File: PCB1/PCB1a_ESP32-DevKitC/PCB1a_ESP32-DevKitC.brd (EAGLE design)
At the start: 125.6 x 84.2 mm, 26 parts, among them J1 691357310006B, J2 618009231421, J3 ESP32_DEVC_MIN_LEFT, J4 ESP32_DEVC_MIN_RIGHT, U2 MAX232D, U4 TLE9250VSJ, U8 74AHCT245, U9 74AHCT245

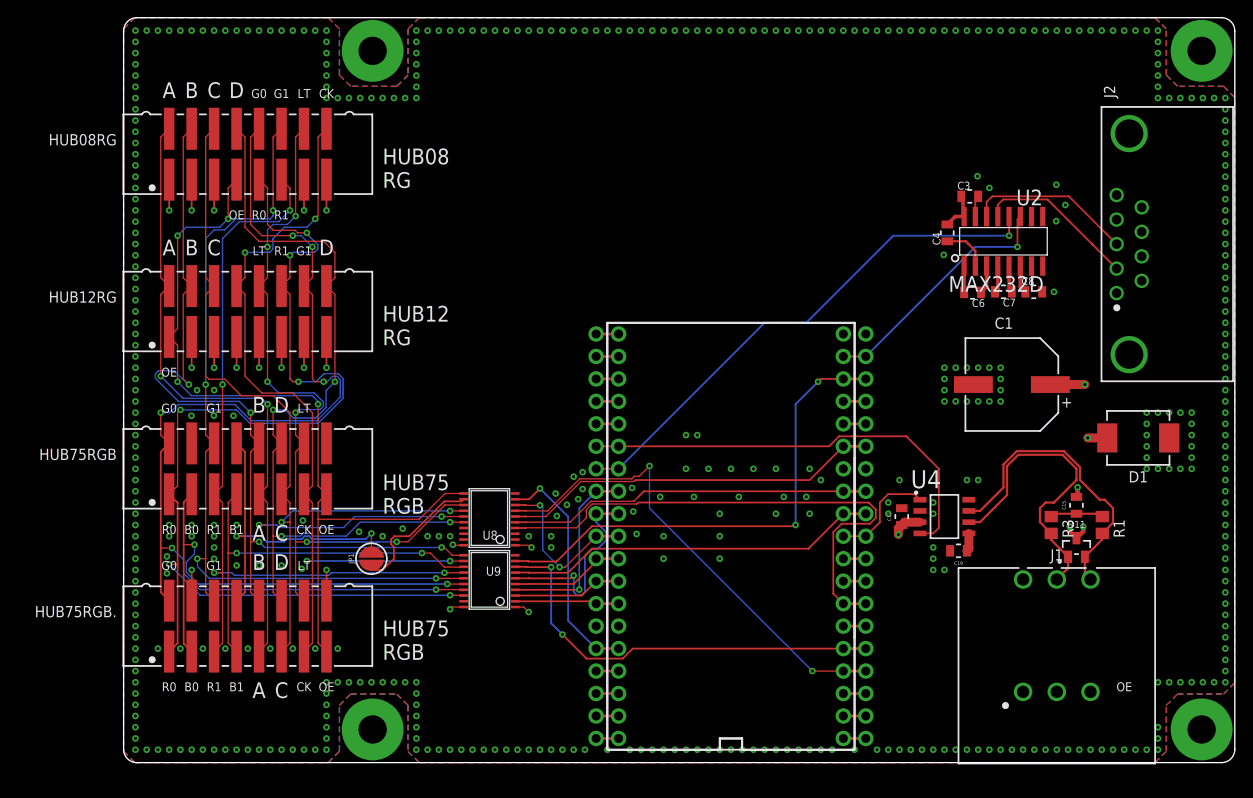
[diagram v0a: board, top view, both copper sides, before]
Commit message: SMD Connectors.
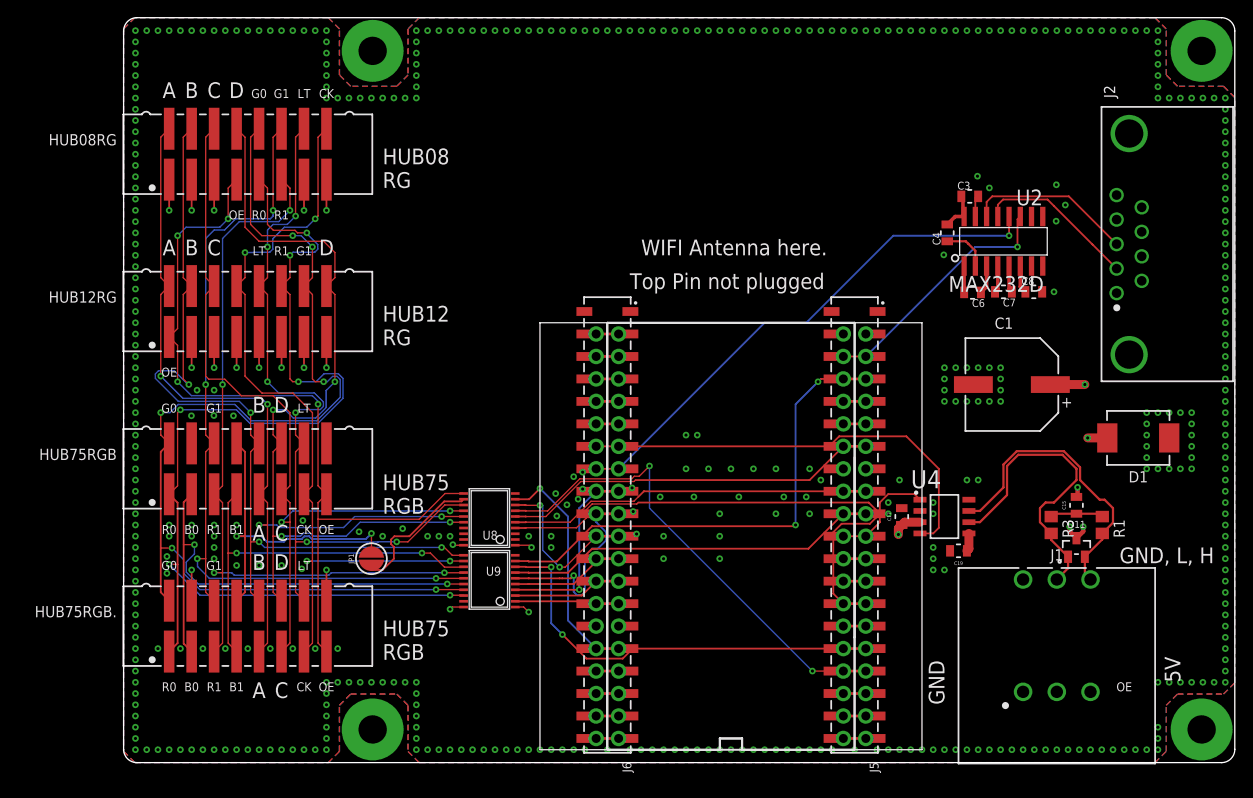
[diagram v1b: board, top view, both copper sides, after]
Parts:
- added J5, J6: 61004021821, Wurth_Connectors_WR-PHD:61004021821
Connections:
- new net N$12: J5.1, J5.2
- new net N$18: J6.1, J6.2
- new net N$4: J3.GND1A, J3.GND1B, J5.3, J5.4
- net +5V: now also J6.39, J6.40
- net 3V3: now also J6.3, J6.4
- net ADDRA_3V: now also J5.17, J5.18
- net ADDRB_3V: now also J5.7, J5.8
- net ADDRC_3V: now also J5.13, J5.14
- net ADDRD_3V: now also J5.27, J5.28
- net ADDRE_3V: now also J6.21, J6.22
- net B1_3V: now also J6.17, J6.18
- net B2_3V: now also J5.19, J5.20
- net CAN1_RXD: now also J6.13, J6.14
- net CAN1_TXD: now also J5.21, J5.22
- net CLK_3V: now also J5.31, J5.32
- net G1_3V: now also J6.25, J6.26
- net G2_3V: now also J6.23, J6.24
- net GND: now also J5.15, J5.16, J6.29, J6.30; no longer J3.GND1A, J3.GND1B
- net LAT_3V: now also J5.33, J5.34
- net N$1: now also J5.29, J5.30
- net N$10: now also J6.7, J6.8
- net N$11: now also J6.11, J6.12
- net N$13: now also J6.5, J6.6
- net N$14: now also J5.10, J5.9
- net N$15: now also J5.11, J5.12
- net N$16: now also J5.23, J5.24
- net N$17: now also J5.25, J5.26
- net N$2: now also J6.37, J6.38
- net N$3: now also J6.35, J6.36
- net N$5: now also J6.33, J6.34
- net N$6: now also J5.39, J5.40
- net N$7: now also J5.37, J5.38
- net N$8: now also J5.35, J5.36
- net N$9: now also J6.10, J6.9
- net OE_3V: now also J6.31, J6.32
- net R1_3V: now also J6.27, J6.28
- net R2_3V: now also J6.19, J6.20
- net RX: now also J6.15, J6.16
- net TX: now also J5.5, J5.6
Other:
- board text added: "5V"
- board text added: "GND"
- board text added: "GND, L, H"
- board text added: "Top Pin not plugged"
- board text added: "WIFI Antenna here."

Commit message: rm THT
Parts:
- removed J3: ESP32_DEVC_MIN_LEFT, eclibrary:ESP32_DEVC_DUAL_HEADER_BOT_MOUNT_LEFT
- removed J4: ESP32_DEVC_MIN_RIGHT, eclibrary:ESP32_DEVC_DUAL_HEADER_BOT_MOUNT_RIGHT
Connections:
- net +5V: no longer J4.5V_A, J4.5V_B
- net 3V3: no longer J4.3V3A, J4.3V3B
- net ADDRA_3V: no longer J3.19A_A, J3.19B_B
- net ADDRB_3V: no longer J3.22A, J3.22B
- net ADDRC_3V: no longer J3.21A, J3.21B
- net ADDRD_3V: no longer J3.4A, J3.4B
- net ADDRE_3V: no longer J4.26A, J4.26B
- net B1_3V: no longer J4.33A, J4.33B
- net B2_3V: no longer J3.18A_A, J3.18B_B
- net CAN1_RXD: no longer J4.35A, J4.35B
- net CAN1_TXD: no longer J3.5A, J3.5B
- net CLK_3V: no longer J3.2A, J3.2B
- net G1_3V: no longer J4.14A_A, J4.14B_B
- net G2_3V: no longer J4.27A, J4.27B
- net GND: no longer J3.GNDA, J3.GNDB, J4.GNDA, J4.GNDB
- net LAT_3V: no longer J3.15A_A, J3.15B_B
- net N$1: no longer J3.0A, J3.0B
- net N$10: no longer J4.VPA, J4.VPB
- net N$11: no longer J4.34A, J4.34B
- net N$13: no longer J4.ENA, J4.ENB
- net N$14: no longer J3.TXA, J3.TXB
- net N$15: no longer J3.RXA, J3.RXB
- net N$16: no longer J3.17A_A, J3.17B_B
- net N$17: no longer J3.16A_A, J3.16_B
- net N$2: no longer J4.CMD_A, J4.CMD_B
- net N$3: no longer J4.D3_A, J4.D3_B
- net N$4: no longer J3.GND1A, J3.GND1B
- net N$5: no longer J4.D2A, J4.D2B
- net N$6: no longer J3.CLKA, J3.CLKB
- net N$7: no longer J3.D0A, J3.D0B
- net N$8: no longer J3.D1A, J3.D1B
- net N$9: no longer J4.VNA, J4.VNB
- net OE_3V: no longer J4.13A_A, J4.13B_B
- net R1_3V: no longer J4.12A, J4.12B
- net R2_3V: no longer J4.25A, J4.25B
- net RX: no longer J4.32A, J4.32B
- net TX: no longer J3.23A, J3.23B
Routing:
- net CLK_3V: track 48.1 -> 21.8 mm
- net CAN1_RXD: track 49.8 -> 23.4 mm
- net RX: track 59.8 -> 33.9 mm
- net ADDRA_3V: track 41.1 -> 16.0 mm
- net TX: track 28.4 -> 8.33 mm
- net B2_3V: track 42.4 -> 34.3 mm
- net ADDRC_3V: track 42.9 -> 35.0 mm
- net ADDRE_3V: track 19.0 -> 11.5 mm
- net OE_3V: track 26.6 -> 19.5 mm
- net LAT_3V: track 54.1 -> 48.1 mm
- net B1_3V: track 21.7 -> 16.5 mm
- net G1_3V: track 12.4 -> 7.52 mm
- net CAN1_TXD: track 12.2 -> 7.42 mm
- net ADDRD_3V: track 60.3 -> 56.2 mm
- net R2_3V: track 23.4 -> 19.9 mm
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
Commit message: ..
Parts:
- added C2, C5: 100nF, Wurth_Capacitors_WCAP-CSGP:WCAP-CSGP_0805_H0.8_R
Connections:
- removed net 3V3: J6.3, J6.4
- removed net VCC: C3.1, C4.2, U2.16
- net +3V3: now also C3.1, C4.2, J6.3, J6.4, U2.16
- net +5V: now also C2.2, C5.2
- net GND: now also C2.1, C5.1
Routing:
- net +3V3: track 2.06 -> 118.6 mm, vias 0 -> 3
- net RX: track 33.9 -> 63.9 mm, vias 1 -> 2
- net CAN1_RXD: track 23.4 -> 51.1 mm
- net CLK_3V: track 21.8 -> 48.5 mm
- net TX: track 8.33 -> 31.9 mm, vias 1 -> 2
- net ADDRA_3V: track 16.0 -> 39.0 mm
- net +5V: track 16.1 -> 32.1 mm, vias 7 -> 9
- net B1_3V: track 16.5 -> 5.20 mm, vias 1 -> 0
- net B2_3V: track 34.3 -> 44.6 mm
- net ADDRD_3V: track 56.2 -> 46.1 mm, vias 0 -> 2
- net OE_3V: track 19.5 -> 29.3 mm, vias 1 -> 2
- net LAT_3V: track 48.1 -> 57.8 mm
- net CAN1_TXD: track 7.42 -> 16.5 mm, vias 0 -> 2
- net R2_3V: track 19.9 -> 11.5 mm, vias 1 -> 0
- net R1_3V: track 8.88 -> 14.1 mm
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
